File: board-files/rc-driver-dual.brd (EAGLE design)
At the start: 29.6 x 17.5 mm, 20 parts

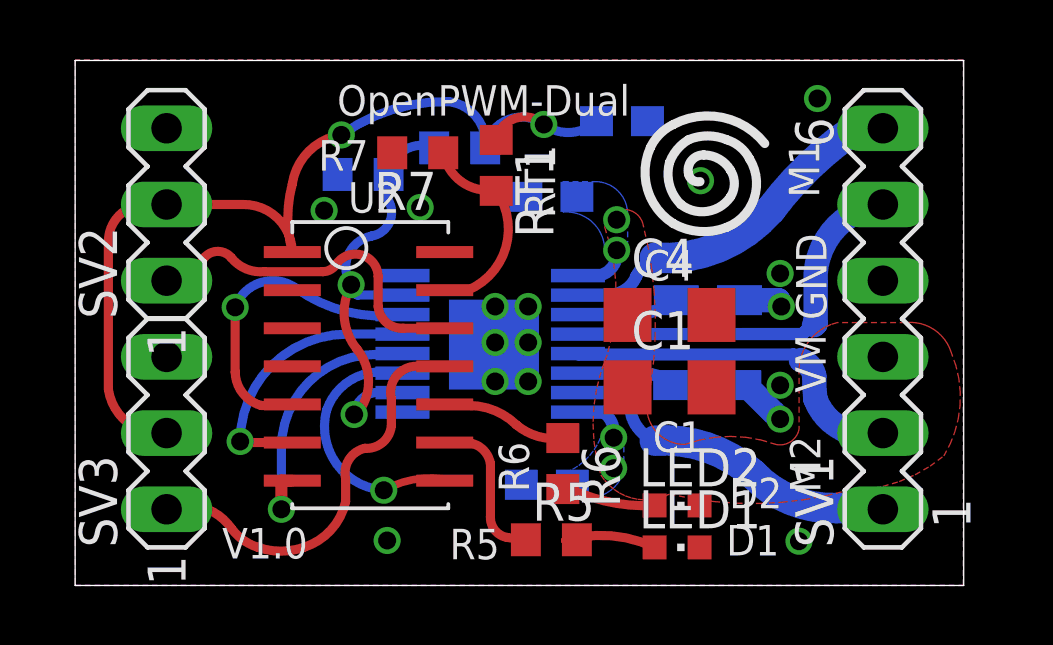
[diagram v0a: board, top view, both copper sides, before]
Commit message: Adding some final touches to the boards. Converting fonts to Vector.
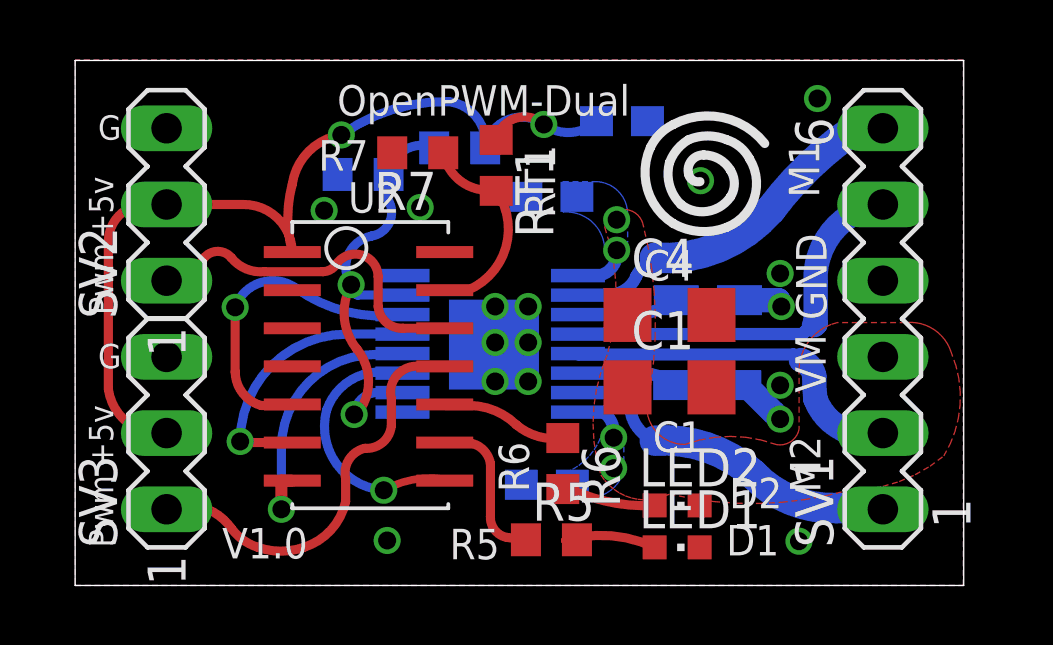
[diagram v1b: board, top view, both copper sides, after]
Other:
- board text added: "+5v"
- board text added: "G"
- board text added: "Pwm"
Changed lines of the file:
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@@
 <grid distance="5" unitdist="mil" unit="mil" style="lines" multiple="1" display="no" altdistance="0.635" altunitdist="mm" altunit="mm"/>
 <layers>
-<layer number="1" name="Top" color="4" fill="1" visible="no" active="yes"/>
+<layer number="1" name="Top" color="4" fill="1" visible="yes" active="yes"/>
 <layer number="2" name="Route2" color="1" fill="3" visible="no" active="yes"/>
 <layer number="3" name="Route3" color="4" fill="3" visible="no" active="yes"/>
@@
 <layer number="19" name="Unrouted" color="6" fill="1" visible="yes" active="yes"/>
 <layer number="20" name="Dimension" color="15" fill="1" visible="yes" active="yes"/>
-<layer number="21" name="tPlace" color="7" fill="1" visible="no" active="yes"/>
-<layer number="22" name="bPlace" color="7" fill="1" visible="yes" active="yes"/>
+<layer number="21" name="tPlace" color="7" fill="1" visible="yes" active="yes"/>
+<layer number="22" name="bPlace" color="7" fill="1" visible="no" active="yes"/>
 <layer number="23" name="tOrigins" color="15" fill="1" visible="yes" active="yes"/>
 <layer number="24" name="bOrigins" color="15" fill="1" visible="yes" active="yes"/>
@@
 <layer number="27" name="tValues" color="7" fill="1" visible="no" active="yes"/>
 <layer number="28" name="bValues" color="7" fill="1" visible="no" active="yes"/>
-<layer number="29" name="tStop" color="7" fill="3" visible="no" active="yes"/>
-<layer number="30" name="bStop" color="7" fill="6" visible="yes" active="yes"/>
+<layer number="29" name="tStop" color="7" fill="3" visible="yes" active="yes"/>
+<layer number="30" name="bStop" color="7" fill="6" visible="no" active="yes"/>
 <layer number="31" name="tCream" color="7" fill="4" visible="no" active="yes"/>
 <layer number="32" name="bCream" color="7" fill="5" visible="no" active="yes"/>
@@
 <text x="14.063" y="12.197" size="1.016" layer="22" font="vector" ratio="18" rot="MR0">C5</text>
 <text x="17.111" y="1.148" size="1.016" layer="22" font="vector" ratio="18" rot="MR0">C3</text>
+<rectangle x1="13.716" y1="6.477" x2="15.367" y2="9.525" layer="29"/>
+<text x="0.762" y="14.859" size="0.8128" layer="21" font="vector" ratio="15">G</text>
+<text x="0.762" y="7.239" size="0.8128" layer="21" font="vector" ratio="15">G</text>
+<text x="1.27" y="1.27" size="0.8128" layer="21" font="vector" ratio="15" rot="R90">Pwm</text>
+<text x="1.27" y="9.017" size="0.8128" layer="21" font="vector" ratio="15" rot="R90">Pwm</text>
+<text x="1.27" y="11.557" size="0.8128" layer="21" font="vector" ratio="15" rot="R90">+5v</text>
+<text x="1.27" y="3.937" size="0.8128" layer="21" font="vector" ratio="15" rot="R90">+5v</text>
 </plain>
 <attributes>
